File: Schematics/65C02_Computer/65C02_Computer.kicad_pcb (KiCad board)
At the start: 2 copper layers, 203.2 x 149.9 mm, 62 parts, among them J1 CLK Jumper, J2 Expansion port, J3 USB_B_Micro, J4 LCD Connector, J5 VIA2PA, J6 VIA2PB, J7 Mini-DIN-6, SW1 RESET, U1 74HC02, U10 FT230XS, U11 65C51N, U12 ATtiny4313-PU, U2 28C256, U3 65C02S, U4 74HC00, U5 74HC21, U6 62256, U7 NE555, U8 65C22S, U9 65C22S, X1 1MHz, X2 1.8432MHz

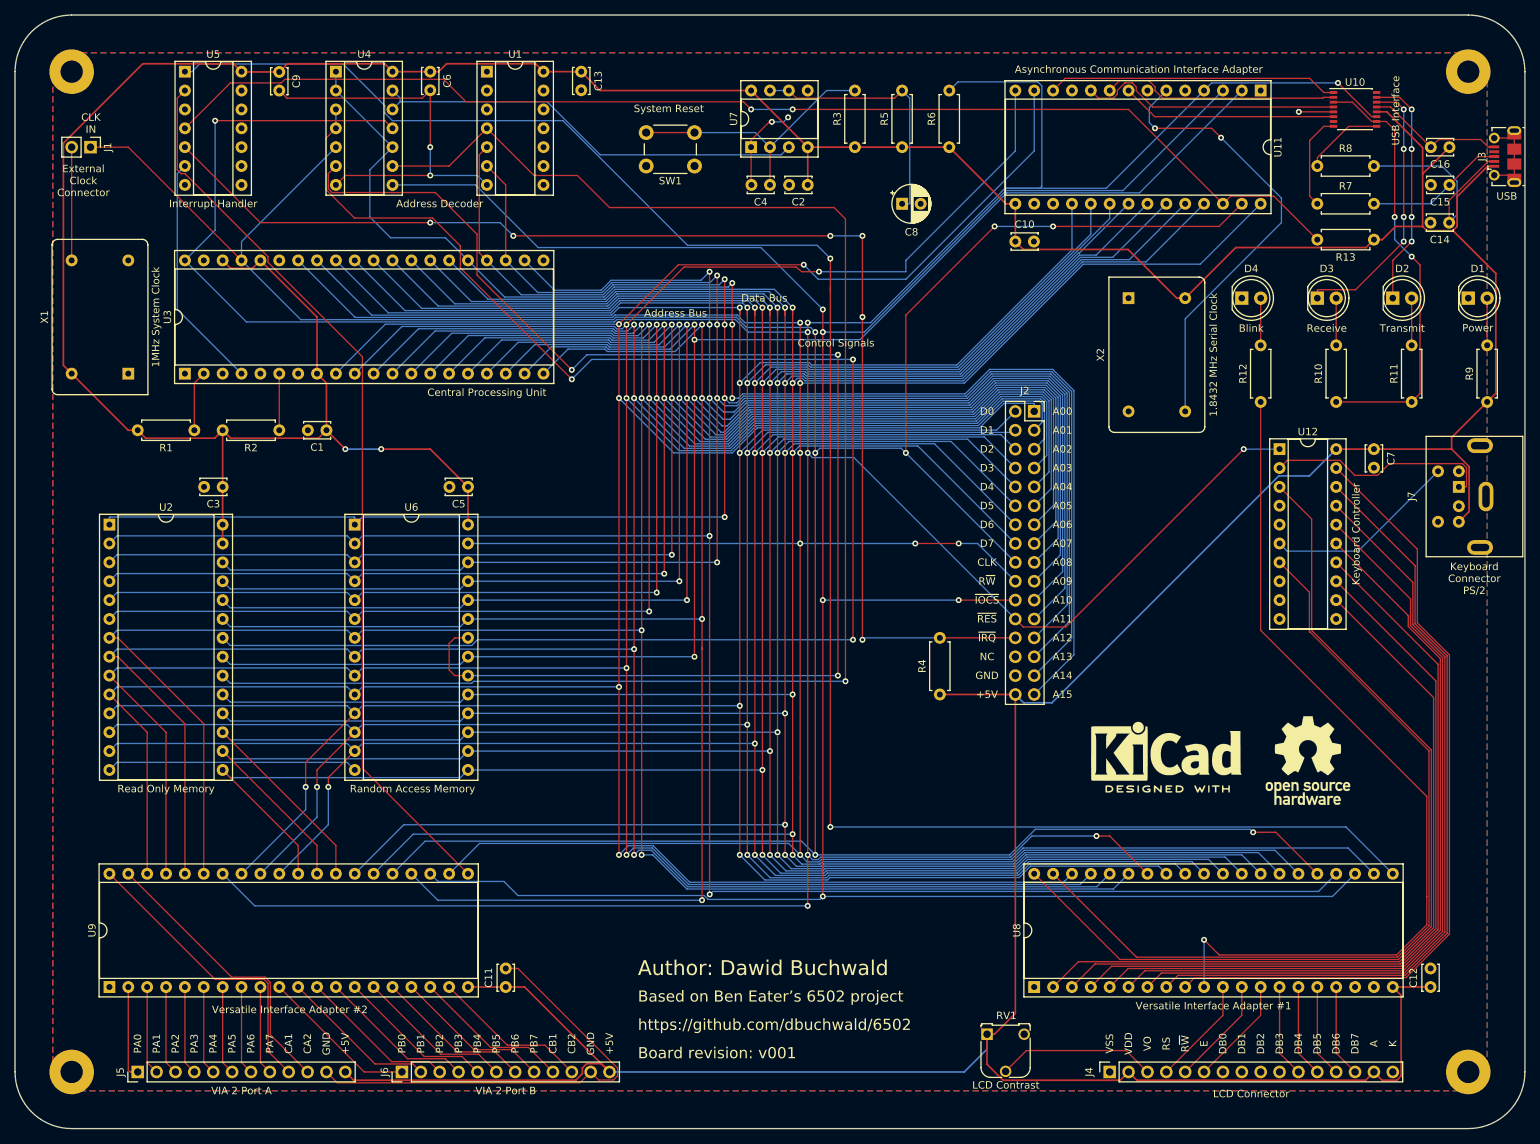
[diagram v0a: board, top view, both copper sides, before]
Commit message: Reordered PCB components
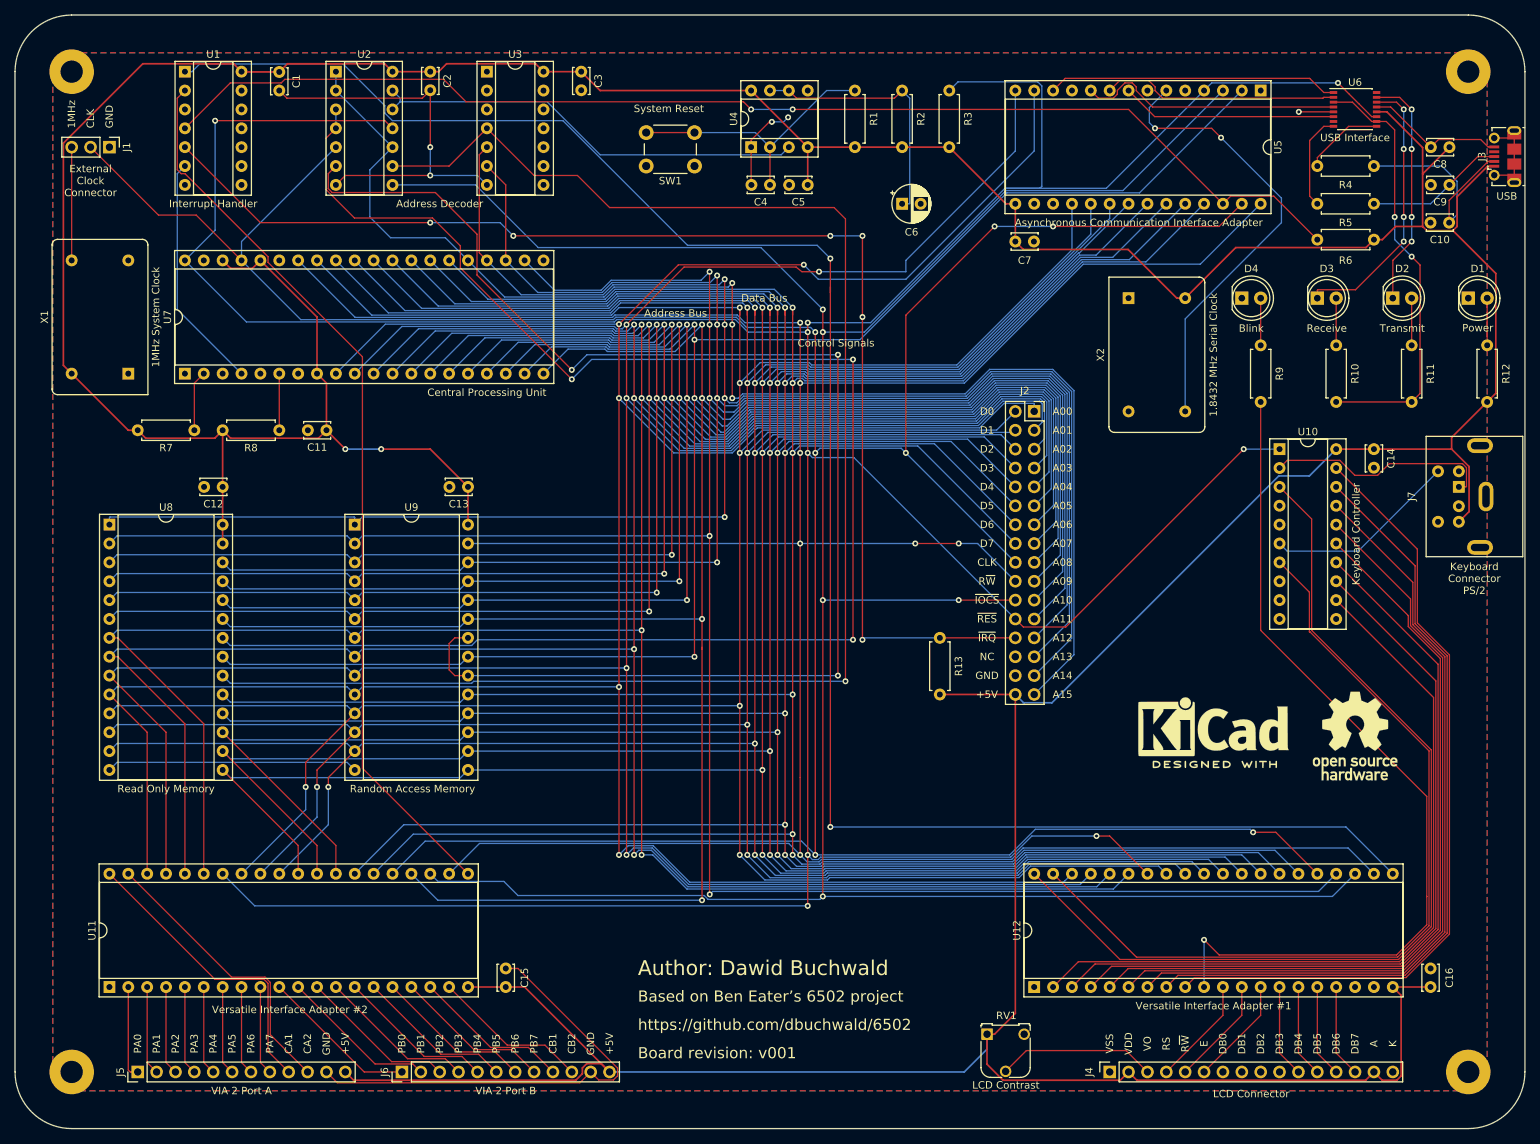
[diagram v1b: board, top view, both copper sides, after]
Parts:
- J1: footprint Connector_PinHeader_2.54mm:PinHeader_1x02_P2.54mm_Vertical -> Connector_PinHeader_2.54mm:PinHeader_1x03_P2.54mm_Vertical
- moved REF** 7.16 mm to (198.1, 117.3)
- moved REF** 7.16 mm to (179.1, 116.1)
- moved J1 2.54 mm to (30.5, 38.1)
- renumbered C9 to C1, C14 to C10, C1 to C11, C3 to C12, C5 to C13, C7 to C14, C11 to C15, C12 to C16, C6 to C2, C13 to C3, C2 to C5, C8 to C6, C10 to C7, C16 to C8, C15 to C9, R3 to R1, R9 to R12, R4 to R13, R5 to R2, R6 to R3, R8 to R4, R7 to R5, R13 to R6, R1 to R7, R2 to R8, R12 to R9, U5 to U1, U12 to U10, U9 to U11, U8 to U12, U4 to U2, U1 to U3, U7 to U4, U11 to U5, U10 to U6, U3 to U7, U2 to U8, U6 to U9
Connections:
- J1 pad 1: CLK -> GND
- J1 pad 2: CLKOUT -> CLK
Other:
- board text added: "1MHz"
- board text removed: "CLK IN"

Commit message: Redesign in progress
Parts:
- added J10: USB_B, Connector_USB:USB_B_OST_USB-B1HSxx_Horizontal, F.Cu at (205.7, 54.6)
- added J8: Optional UART Port, Connector_PinSocket_2.54mm:PinSocket_1x06_P2.54mm_Vertical, F.Cu at (179.1, 27.9)
- added J9: Power Connector, Connector_BarrelJack:BarrelJack_Horizontal, F.Cu at (207.0, 74.9)
- moved X2 24.1 mm to (167.6, 82.5)
- moved C4 22.5 mm to (102.8, 27.9)
- moved R3 20.5 mm to (123.2, 40.6), turned to 0 degrees
- moved C6 19.4 mm to (118.1, 41.9), turned to 180 degrees
- moved D1 19.1 mm to (194.3, 59.7)
- moved R10 19.1 mm to (176.5, 73.7)
- moved R11 19.1 mm to (186.7, 73.7)
- moved R12 19.1 mm to (196.8, 73.7)
- moved D2 19.1 mm to (184.2, 59.7)
- moved D3 19.1 mm to (174.0, 59.7)
- moved D4 19.1 mm to (163.8, 59.7)
- moved R9 19.1 mm to (166.4, 73.7)
- moved C5 16.7 mm to (108.0, 40.6), turned to 0 degrees
- moved C7 14.2 mm to (138.4, 48.3)
- moved U5 14.2 mm to (171.4, 27.9)
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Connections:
- C10 pad 1: Net-(C10-Pad1) -> USBD-
- C9 pad 1: Net-(C9-Pad1) -> USBD+
- J3 pad 2: Net-(C10-Pad1) -> USBD-
- J3 pad 3: Net-(C9-Pad1) -> USBD+
- R4 pad 2: Net-(C10-Pad1) -> Net-(R4-Pad2)
- R5 pad 2: Net-(C9-Pad1) -> Net-(R5-Pad2)
- U6 pad 8: USBD+ -> Net-(R5-Pad2)
- U6 pad 9: USBD- -> Net-(R4-Pad2)
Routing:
- net +5V: track 772.6 -> 635.1 mm
- net ~AIRQ: track 164.9 -> 41.8 mm, vias 2 -> 0
- net ~RES: track 548.0 -> 443.9 mm, vias 9 -> 8
- net a10: track 306.0 -> 240.8 mm
- net ~IOCS: track 364.4 -> 302.7 mm
- net ~ROM_CS: track 214.9 -> 161.6 mm
- net CLK: track 433.6 -> 382.2 mm, vias 7 -> 5
- net R~W: track 420.1 -> 370.2 mm
- net a0: track 410.4 -> 366.0 mm
- net d7: track 432.9 -> 390.6 mm
- net a1: track 414.7 -> 372.6 mm
- net d6: track 432.6 -> 392.9 mm
- net RxD: track 39.2 -> 0.00 mm
- net d5: track 395.0 -> 357.8 mm
- net Net-(C4-Pad1): track 37.1 -> 0.00 mm
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
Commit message: PCB RC1
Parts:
- moved J2 1.27 mm to (180.3, 27.9)
- renumbered J4 to J10, J8 to J2, J10 to J4, J9 to J5, J7 to J6, J2 to J7, J5 to J8, J6 to J9
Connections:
- C10 pad 1: USBD- -> PUSBD-
- C9 pad 1: USBD+ -> PUSBD+
- J3 pad 2: USBD- -> PUSBD-
- J3 pad 3: USBD+ -> PUSBD+
- J4 pad 2: USBD- -> PUSBD-
- J4 pad 3: USBD+ -> PUSBD+
- R4 pad 2: Net-(R4-Pad2) -> PUSBD-
- R5 pad 2: Net-(R5-Pad2) -> PUSBD+
- U6 pad 8: Net-(R5-Pad2) -> USBD+
- U6 pad 9: Net-(R4-Pad2) -> USBD-
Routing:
- net +5V: track 635.1 -> 837.3 mm, vias 2 -> 3
- net ~AIRQ: track 41.8 -> 157.9 mm
- net ~RES: track 443.9 -> 533.5 mm, vias 8 -> 9
- net a10: track 240.8 -> 301.4 mm, vias 4 -> 6
- net ~IOCS: track 302.7 -> 358.4 mm, vias 5 -> 7
- net ~ROM_CS: track 161.6 -> 216.2 mm
- net PUSBD+: track 0.00 -> 51.5 mm, vias 0 -> 1
- net RxD: track 0.00 -> 47.4 mm, vias 0 -> 3
- net ~CTS: track 0.00 -> 46.2 mm, vias 0 -> 2
- net PUSBD-: track 0.00 -> 42.7 mm, vias 0 -> 1
- net RS232CLK: track 39.3 -> 80.7 mm
- net CLK: track 382.2 -> 421.9 mm, vias 5 -> 6
- net TxD: track 0.00 -> 39.3 mm
- net Net-(C4-Pad1): track 0.00 -> 38.5 mm
- net R~W: track 370.2 -> 407.8 mm
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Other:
- board text added: "65C02 Hobby Computer"
- board text added: "Keyboard, LCD and Blink LED"
- board text added: "Power In"
- board text added: "RxD"
- board text added: "System Bus Expansion Port"
- board text added: "TxD"
- board text added: "UART Interface"
- board text added: "~CTS"
- board text added: "~RTS"

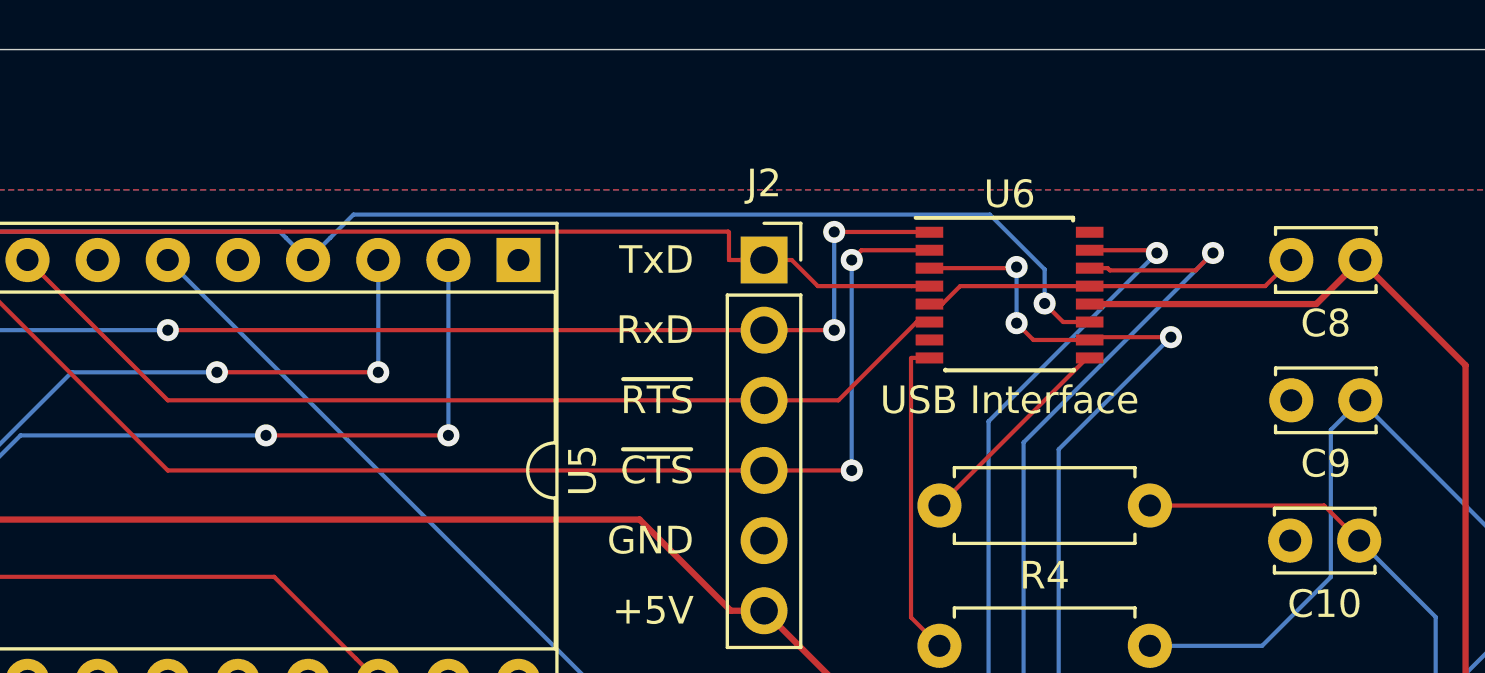
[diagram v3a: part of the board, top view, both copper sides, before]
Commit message: PCB RC2 - updated FT230XS footprint
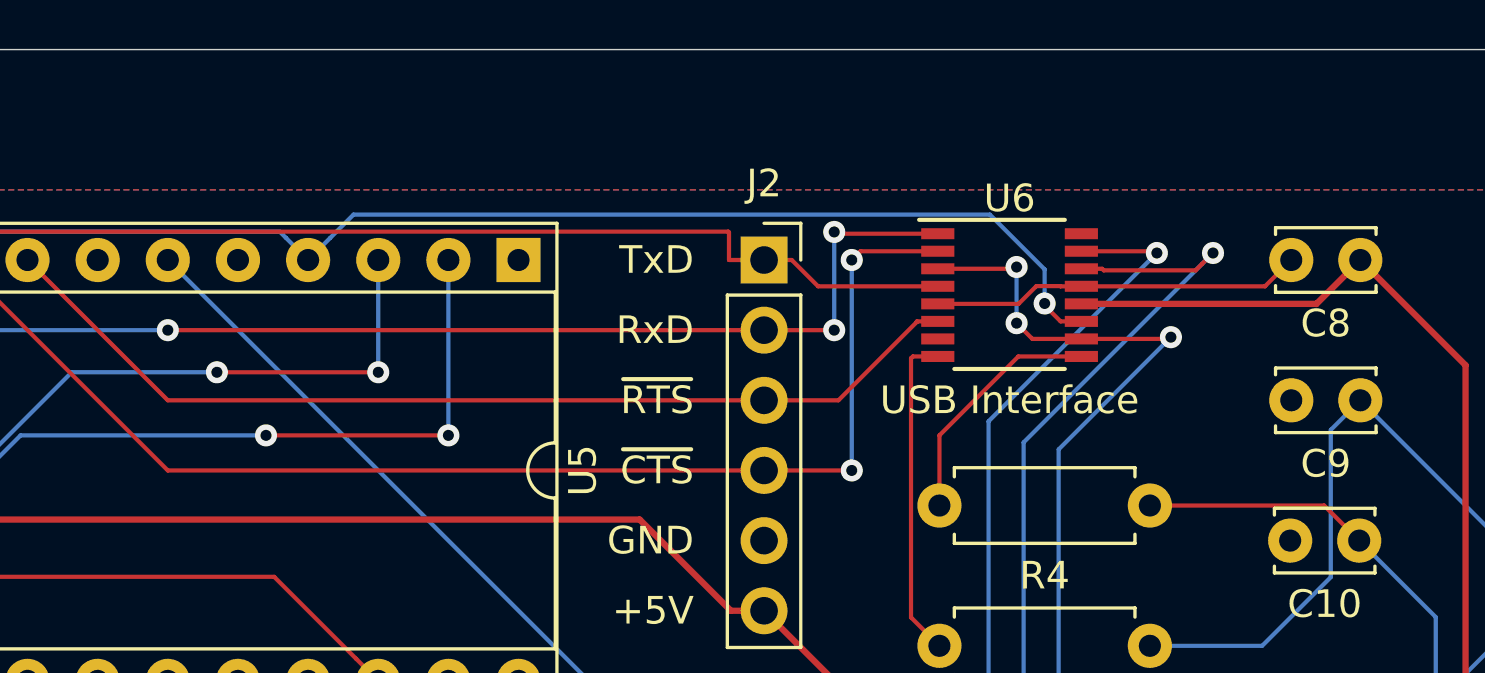
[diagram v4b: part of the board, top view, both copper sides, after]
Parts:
- U6: footprint Package_SO:SSOP-16_4.4x5.2mm_P0.65mm -> Package_SO:SSOP-16_3.9x4.9mm_P0.635mm
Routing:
- net USBD-: track 7.65 -> 8.86 mm
